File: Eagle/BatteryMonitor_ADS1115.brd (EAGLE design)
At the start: 60.6 x 49.5 mm, 15 parts, among them IC1 MCP1703CB

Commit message: Optimize part placement
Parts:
- C2, C3, C5: value 100n -> 1µ
- C4: value 100n -> 2µ
- C7: value 100n -> 10µ
- moved C1 1.80 mm to (26.7, 22.9)
- moved U$2 1.80 mm to (20.3, 14.0)
- moved C2 1.27 mm to (26.7, 3.81)
- moved C5 1.27 mm to (5.71, 24.8)
- moved HSTS016L 1.27 mm to (5.08, 17.8)
- moved IC1 1.27 mm to (5.08, 28.6)
- moved C4 1.27 mm to (36.8, 26.7)
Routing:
- net V5.5: track 45.5 -> 51.1 mm
- net VCC: track 45.4 -> 49.1 mm
- net N$9: track 27.5 -> 30.1 mm
- net N$6: track 11.7 -> 14.0 mm
- net N$4: track 11.7 -> 14.0 mm
- net N$7: track 14.2 -> 15.4 mm

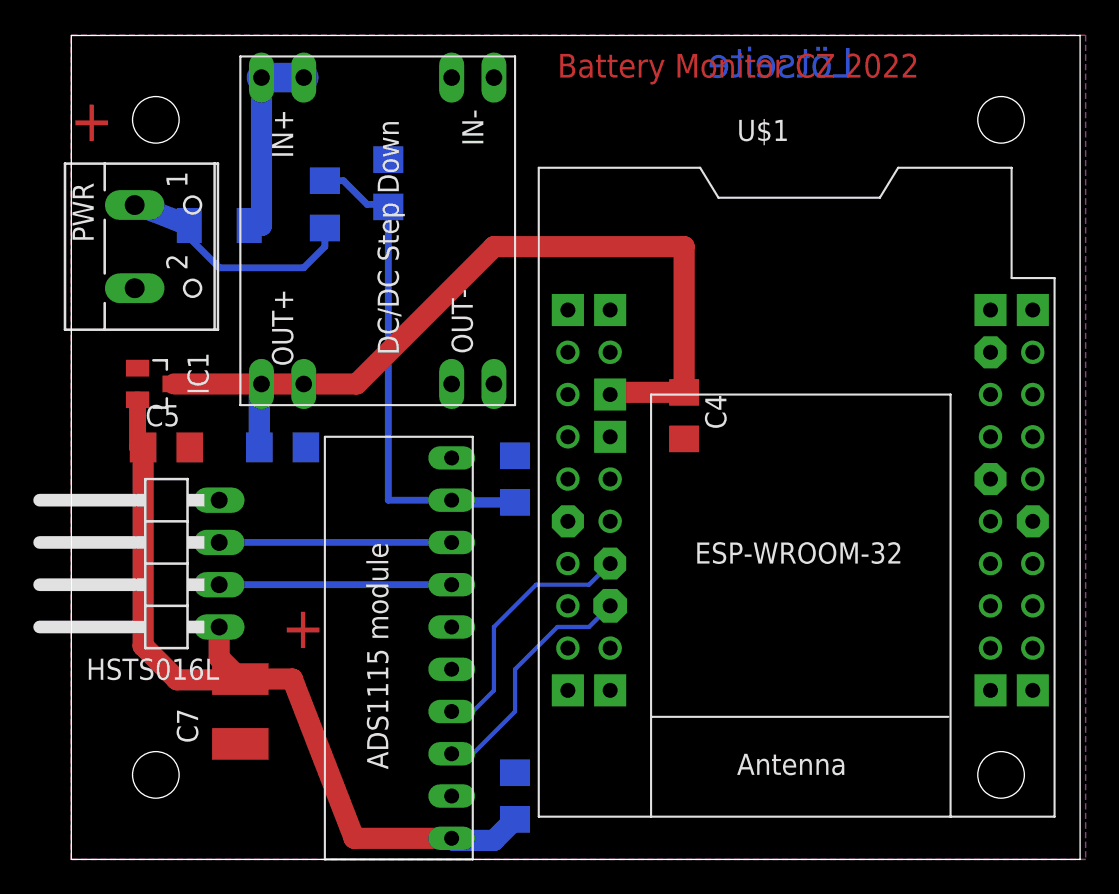
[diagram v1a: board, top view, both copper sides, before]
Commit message: Change layout - all SMD on top
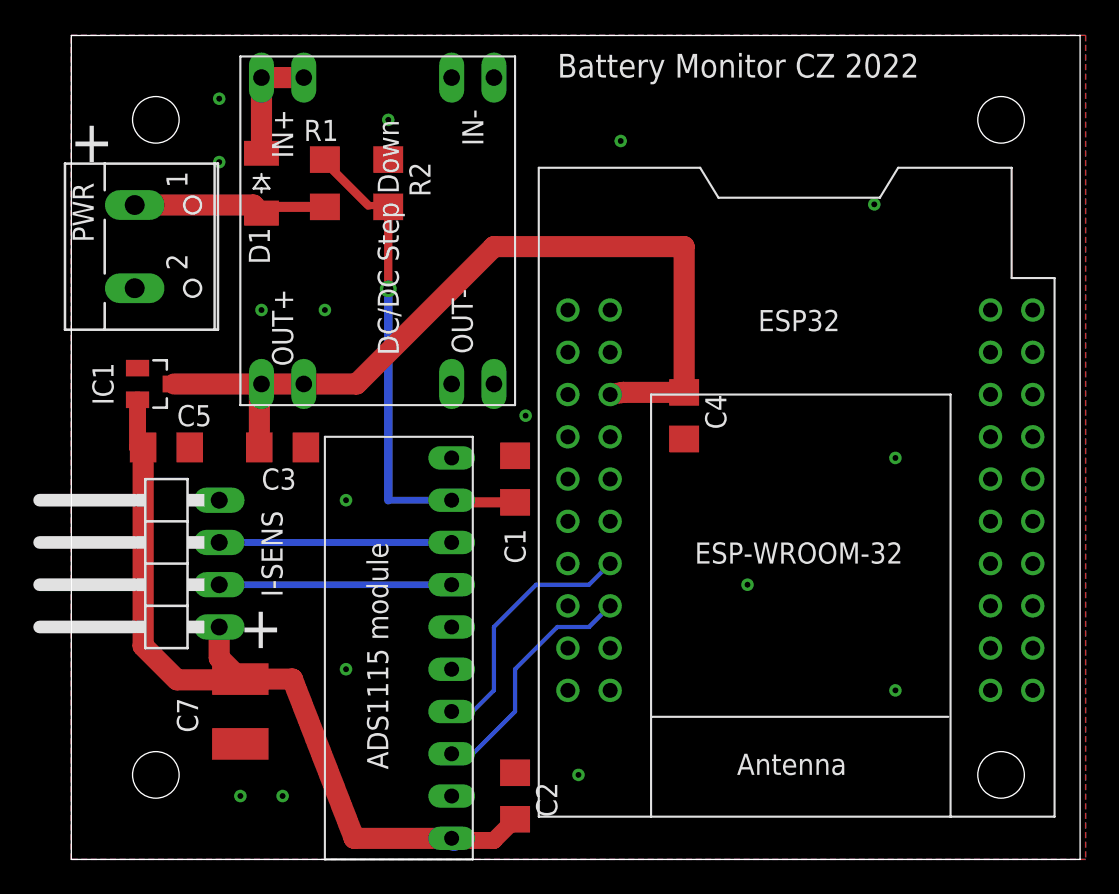
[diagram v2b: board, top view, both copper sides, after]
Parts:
- moved D1 3.59 mm to (11.4, 40.6), flipped to the top, turned to 270 degrees
- moved R1 1.27 mm to (15.2, 40.6), flipped to the top
- flipped C1 to the top
- flipped C2 to the top
- flipped C3 to the top, turned to 0 degrees
- flipped R2 to the top
- renumbered HSTS016L to I-SENS, U$1 to ESP32
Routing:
- net V12: track 12.2 -> 7.09 mm
- net N$1: track 14.8 -> 11.8 mm
- net N$9: track 30.1 -> 31.2 mm, vias 0 -> 1
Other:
- board text removed: "Lötseite"

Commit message: Correct description of DCDC output voltage
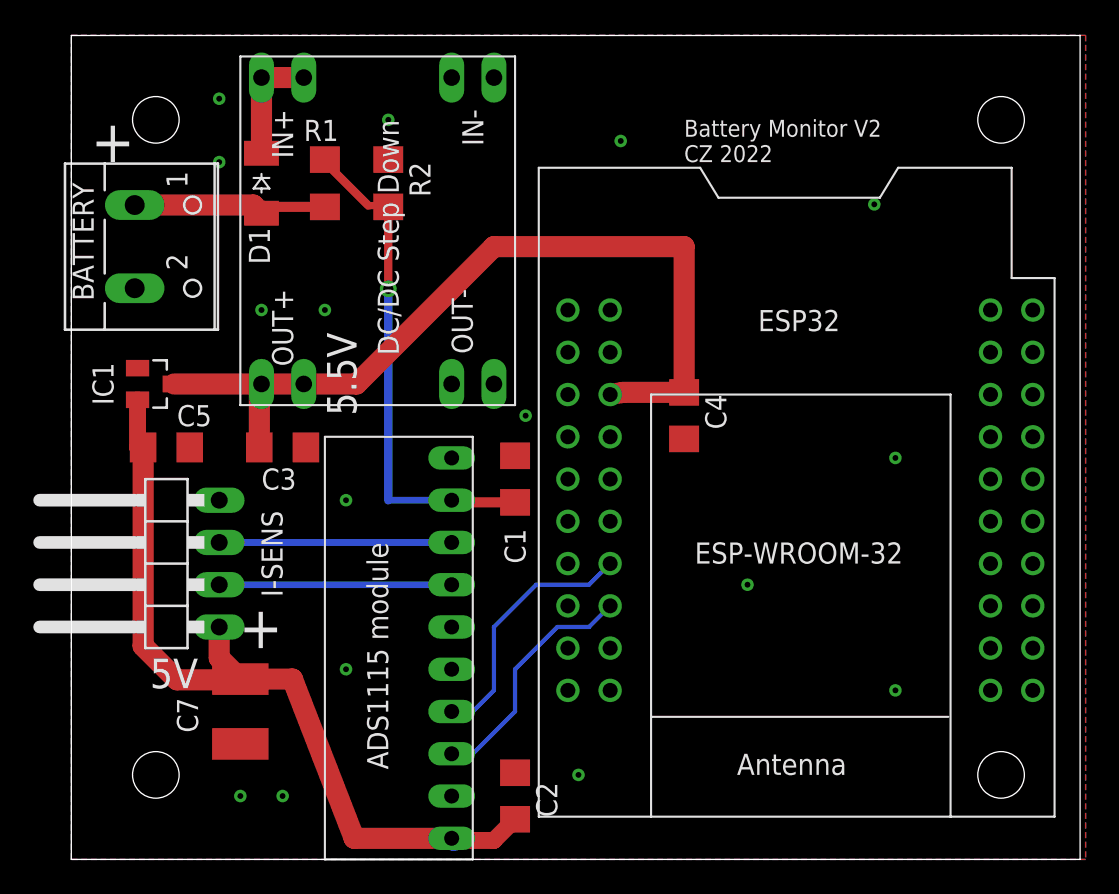
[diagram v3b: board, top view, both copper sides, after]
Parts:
- renumbered PWR to BATTERY
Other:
- board text added: "5.5V"
- board text added: "5V"
- board text added: "Battery Monitor V2 CZ 2022"
- board text removed: "Battery Monitor CZ 2022"
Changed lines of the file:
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@@
 <rectangle x1="7.62" y1="36.83" x2="10.16" y2="39.37" layer="42"/>
 <rectangle x1="6.35" y1="12.7" x2="10.16" y2="20.32" layer="41" rot="R180"/>
-<text x="2.54" y="41.91" size="2.54" layer="25" font="vector" rot="MR0">+</text>
-<text x="29.21" y="46.99" size="1.4224" layer="25" font="vector">Battery Monitor CZ 2022</text>
+<text x="3.81" y="41.91" size="2.54" layer="25" font="vector" rot="MR0">+</text>
+<text x="36.83" y="41.91" size="1.016" layer="25" font="vector">Battery Monitor V2
+CZ 2022</text>
 <text x="12.7" y="12.7" size="2.54" layer="25" font="vector" rot="MR0">+</text>
+<text x="17.145" y="26.67" size="1.778" layer="25" rot="R90">5.5V</text>
+<text x="7.62" y="12.065" size="1.778" layer="25" rot="R180">5V</text>
 </plain>
 <attributes>
@@
 <attribute name="VALUE" x="9.525" y="24.765" size="1.27" layer="27" rot="R180"/>
 </element>
-<element name="PWR" library="con-wago-500" package="W237-102" value="12V" x="5.08" y="36.83" smashed="yes" rot="R270">
+<element name="BATTERY" library="con-wago-500" package="W237-102" value="12V" x="5.08" y="36.83" smashed="yes" rot="R270">
 <attribute name="GND" x="5.08" y="36.83" size="1.778" layer="27" rot="R270" display="off"/>
 <attribute name="MF" value="" x="5.08" y="36.83" size="1.778" layer="27" rot="R270" display="off"/>
@@
 <contactref element="U$3" pad="1"/>
 <contactref element="U$3" pad="2"/>
-<contactref element="PWR" pad="2"/>
+<contactref element="BATTERY" pad="2"/>
 <contactref element="C2" pad="2"/>
 <contactref element="C4" pad="2"/>
@@
 </signal>
 <signal name="N$1">
-<contactref element="PWR" pad="1"/>
+<contactref element="BATTERY" pad="1"/>
 <contactref element="D1" pad="A"/>
 <wire x1="3.85" y1="39.37" x2="3.81" y2="39.33" width="1.27" layer="16"/>
@@
 </board>
 </drawing>
+<compatibility>
+<note version="6.3" minversion="6.2.2" severity="warning">
+Since Version 6.2.2 text objects can contain more than one line,
+which will not be processed correctly with this version.
+</note>
+</compatibility>
 </eagle>

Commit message: Update layout: add 3.3V to IO connector
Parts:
- added IO2, IO4: (no value), con-amp:10X02MTA
- added IO5: (no value), con-amp:10X03MTA
- added R3, R4, R5: 1k, eagle-ltspice:R1206
- C2, C3, C5: value 1µ -> 1u
- C4: value 2µ -> 2u
- C7: value 10µ -> 2u; device resistor:C4532 -> rcl:C1206
- R1: value 31k -> 33k
- moved C7 1.42 mm to (8.89, 9.53)
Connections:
- net N$1 renamed 12V
- net V5.5 renamed V5.8
- new net N$1: IO5.1, R5.1
- new net N$10: IO4.1, R4.1
- new net N$11: IO2.1, R3.1
- new net N$12: ESP32.3V3, IO5.3
- new net N$2: ESP32.IO2, R3.2
- new net N$3: ESP32.IO4, R4.2
- new net N$5: ESP32.IO5, R5.2
- net GND: now also IO2.2, IO4.2, IO5.2
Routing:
- net N$3: track 0.00 -> 28.2 mm
- net N$12: track 0.00 -> 21.3 mm
- net N$5: track 0.00 -> 20.1 mm
- net N$2: track 0.00 -> 16.5 mm, vias 0 -> 1
- net N$10: track 0.00 -> 4.18 mm
- net N$11: track 0.00 -> 3.66 mm
- net N$1: track 0.00 -> 3.66 mm
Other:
- board text added: "12V"
- board text added: "3.3V"
- board text added: "5.8V"
- board text removed: "5.5V"
